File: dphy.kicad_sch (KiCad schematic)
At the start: 5 parts, among them J1901 FFC-22p-P0.5mm, U1901 RCLAMP0524P, U1902 RCLAMP0524P, U1903 RCLAMP0524P, U1904 RCLAMP0524P

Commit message: Further refinements
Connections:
- net CAM_GPIO0 renamed P17
- net CAM_GPIO1 renamed P18
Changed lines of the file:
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@@
 		)
 	)
-	(hierarchical_label "CAM_GPIO1"
+	(hierarchical_label "P18"
 		(shape input)
 		(at 193.04 109.22 180)
@@
 		)
 	)
-	(hierarchical_label "CAM_GPIO1"
+	(hierarchical_label "P18"
 		(shape input)
 		(at 116.84 109.22 0)
@@
 		)
 	)
-	(hierarchical_label "CAM_GPIO0"
+	(hierarchical_label "P17"
 		(shape input)
 		(at 116.84 104.14 0)
@@
 		)
 	)
-	(hierarchical_label "CAM_GPIO0"
+	(hierarchical_label "P17"
 		(shape input)
 		(at 193.04 106.68 180)
@@
 				)
 				(hide yes)
+			)
+		)
+		(property "LCSC Part" ""
+			(at 90.17 138.43 0)
+			(effects
+				(font
+					(size 1.27 1.27)
+				)
+			)
+		)
+		(property "Sim.Enable" ""
+			(at 90.17 138.43 0)
+			(effects
+				(font
+					(size 1.27 1.27)
+				)
 			)
 		)
@@
 			)
 		)
+		(property "LCSC Part" ""
+			(at 90.17 73.66 0)
+			(effects
+				(font
+					(size 1.27 1.27)
+				)
+			)
+		)
+		(property "Sim.Enable" ""
+			(at 90.17 73.66 0)
+			(effects
+				(font
+					(size 1.27 1.27)
+				)
+			)
+		)
 		(pin "1"
 		)
@@
 				)
 				(hide yes)
+			)
+		)
+		(property "LCSC Part" ""
+			(at 90.17 41.91 0)
+			(effects
+				(font
+					(size 1.27 1.27)
+				)
+			)
+		)
+		(property "Sim.Enable" ""
+			(at 90.17 41.91 0)
+			(effects
+				(font
+					(size 1.27 1.27)
+				)
 			)
 		)
@@
 			)
 		)
+		(property "LCSC Part" ""
+			(at 214.63 91.44 0)
+			(effects
+				(font
+					(size 1.27 1.27)
+				)
+			)
+		)
+		(property "Sim.Enable" ""
+			(at 214.63 91.44 0)
+			(effects
+				(font
+					(size 1.27 1.27)
+				)
+			)
+		)
 		(pin "1"
 		)
@@
 			)
 		)
+		(property "LCSC Part" ""
+			(at 90.17 106.68 0)
+			(effects
+				(font
+					(size 1.27 1.27)
+				)
+			)
+		)
+		(property "Sim.Enable" ""
+			(at 90.17 106.68 0)
+			(effects
+				(font
+					(size 1.27 1.27)
+				)
+			)
+		)

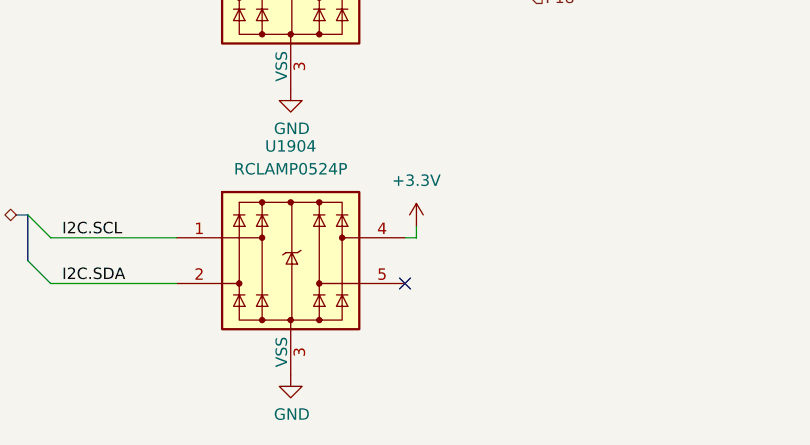
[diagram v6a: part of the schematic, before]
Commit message: Finish transitioning to RP2040
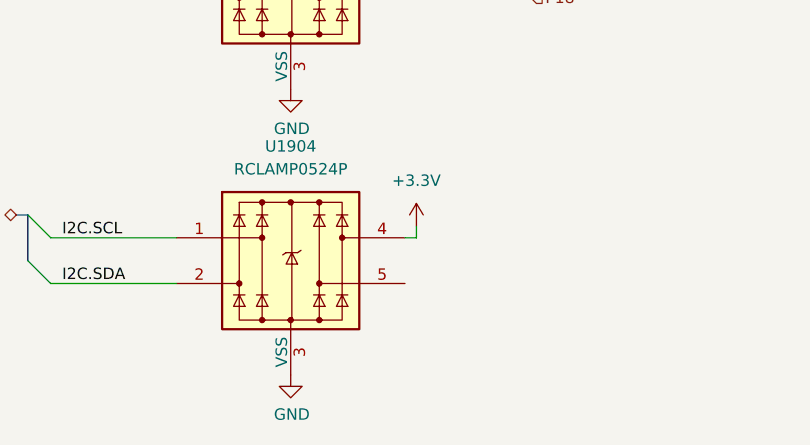
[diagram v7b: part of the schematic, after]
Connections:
- no-connect marks 1 -> 0
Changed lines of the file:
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@@
 		(color 0 0 0 0)
-	)
-	(no_connect
-		(at 102.87 140.97)
 	)
 	(bus_entry

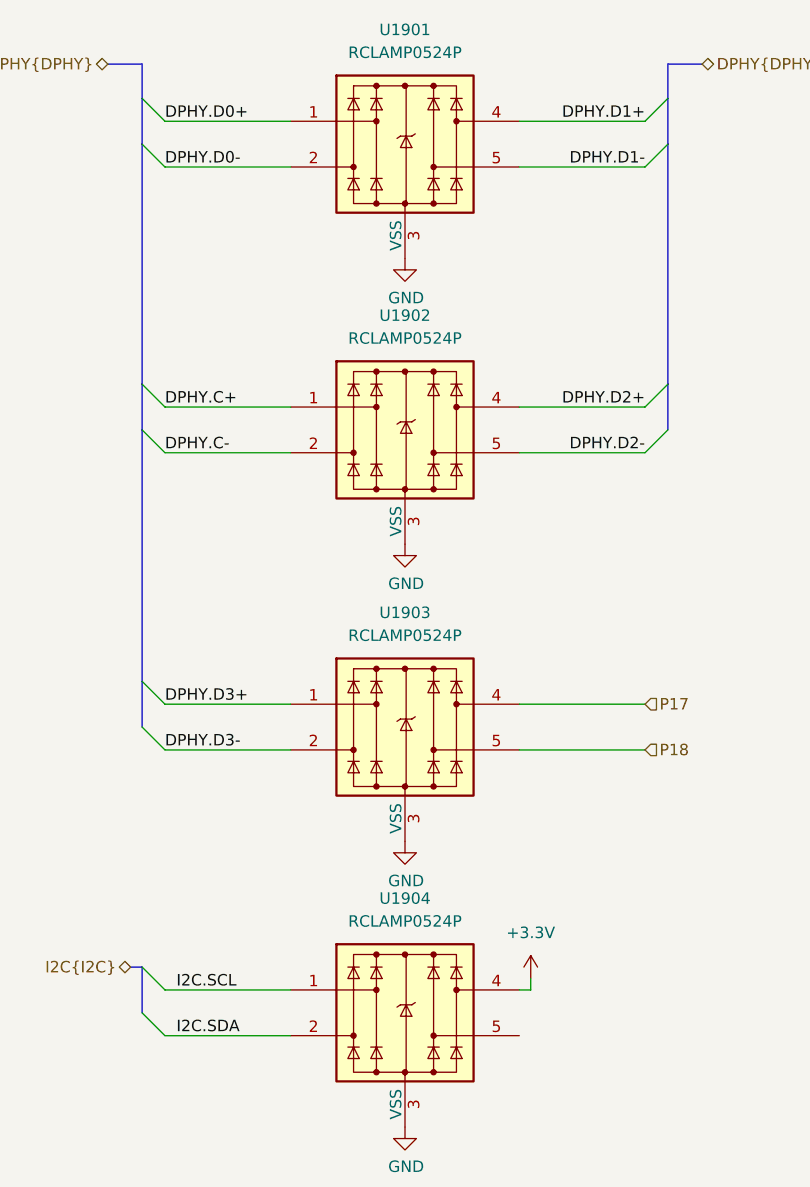
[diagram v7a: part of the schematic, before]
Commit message: Apply part PCBA position corrections
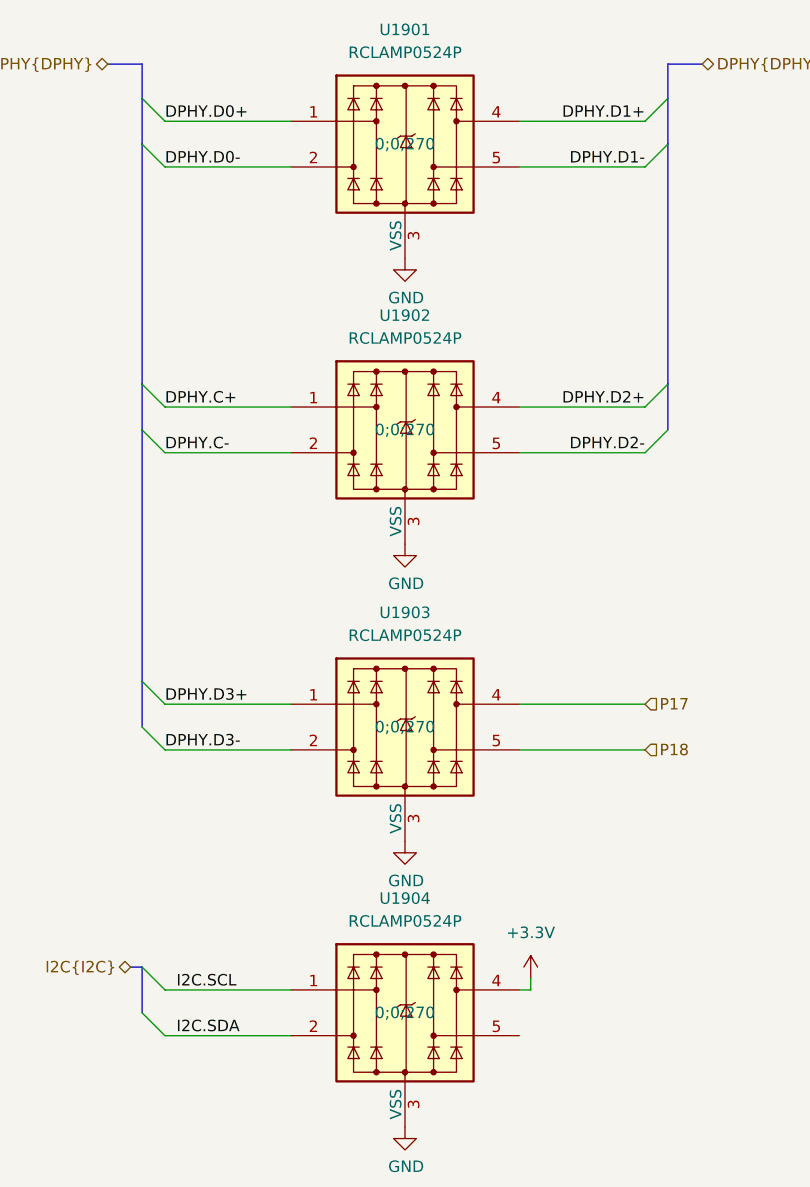
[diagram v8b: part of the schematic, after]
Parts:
- U1901, U1902, U1903, U1904: JLCPCB_CORRECTION (none) -> 0;0;270
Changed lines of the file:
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@@
+			)
+		)
+		(property "JLCPCB_CORRECTION" "0;0;270"
+			(at 90.17 138.43 0)
+			(effects
+				(font
+					(size 1.27 1.27)
+				)
 			)
 		)
@@
 			)
 		)
+		(property "JLCPCB_CORRECTION" "0;0;270"
+			(at 90.17 73.66 0)
+			(effects
+				(font
+					(size 1.27 1.27)
+				)
+			)
+		)
 		(pin "1"
 		)
@@
 		)
 		(property "Sim.Enable" ""
+			(at 90.17 41.91 0)
+			(effects
+				(font
+					(size 1.27 1.27)
+				)
+			)
+		)
+		(property "JLCPCB_CORRECTION" "0;0;270"
 			(at 90.17 41.91 0)
 			(effects
@@
 			(at 90.17 106.68 0)
 			(effects
+				(font
+					(size 1.27 1.27)
+				)
+			)
+		)
+		(property "JLCPCB_CORRECTION" "0;0;270"
+			(at 90.17 106.68 0)
+			(effects
